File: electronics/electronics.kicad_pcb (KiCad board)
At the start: 2 copper layers, 50 parts, among them J1 USB_C_Receptacle_USB2.0_14P, J2 AMT_102, J3 SPARK_MAX, J4 BLDC_FAN_ESC, J5 Power Probes, SW1 RST, SW2 BOOT, SW3 SW_Push, SW4 SW_Push, SW5 SW_Push, SW6 SW_Push, U1 ESP32-S3-WROOM-1, U2 LSF0204, U3 NCP1117-3.3_SOT223, U4 TPS62140, U5 NCP1117-3.3_SOT223, U8 TVS1400DRV, U9 TVS1400DRV

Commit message: ready to ship out
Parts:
- added G***: LOGO, LOGO, B.Cu at (161.2, 101.2)
- added G***: LOGO, LOGO, B.Cu at (117.0, 100.9)
- added G***: LOGO, LOGO, B.Cu at (138.9, 68.7)
- added L1: 2.2uH, Inductor_SMD:L_Vishay_IHLP-1212, F.Cu at (153.8, 94.8)
- C10, C11, C4, C5, C6, C8: footprint Capacitor_SMD:C_0603_1608Metric -> Capacitor_SMD:C_0805_2012Metric
- J5: footprint Connector_PinSocket_2.54mm:PinSocket_1x06_P2.54mm_Vertical -> Connector_PinHeader_2.54mm:PinHeader_1x04_P2.54mm_Vertical
- U7: value ~ -> BMI270
- moved C5 142.2 mm to (167.8, 96.2), turned to 90 degrees
- moved R7 138.8 mm to (167.2, 70.6), turned to 90 degrees
- moved R12 135.4 mm to (173.4, 94.9), turned to 90 degrees
- moved R13 135.3 mm to (173.4, 98.1), turned to 90 degrees
- moved R5 132.4 mm to (166.4, 92.6)
- moved D3 131.7 mm to (171.7, 98.2), turned to -90 degrees
- moved D4 130.1 mm to (171.7, 94.9), turned to -90 degrees
- moved C4 129.1 mm to (155.2, 98.5), turned to -90 degrees
- moved C6 127.6 mm to (153.6, 103.3)
- moved C7 119.1 mm to (149.9, 103.1), turned to 180 degrees
- moved R9 117.7 mm to (150.6, 96.2), turned to 90 degrees
- moved R11 109.6 mm to (148.1, 99.2)
- moved R10 109.5 mm to (148.1, 97.5), turned to 180 degrees
- moved C9 105.9 mm to (136.4, 102.2), turned to -90 degrees
- moved C3 104.9 mm to (130.7, 95.7), turned to 180 degrees
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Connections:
- net Net-(L1-Pad1) renamed /POWER_INDUCTOR
- J5 pad 2: +5V -> +3V3
- J5 pad 3: +3V3 -> GND
- J5 pad 4: +3V3 -> GND
- U1 pad 15: unconnected-(U1-IO3-Pad15) -> /BTN3
- U1 pad 17: unconnected-(U1-IO9-Pad17) -> /BTN4
- U1 pad 18: unconnected-(U1-IO10-Pad18) -> /SCL
- U1 pad 19: unconnected-(U1-IO11-Pad19) -> /SDA
- U1 pad 20: unconnected-(U1-IO12-Pad20) -> /SPARK_MAX_PWM
- U1 pad 25: unconnected-(U1-IO48-Pad25) -> /BTN2
- U1 pad 26: unconnected-(U1-IO45-Pad26) -> /BTN1
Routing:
- net +3V3: track 40.4 -> 269.7 mm, vias 0 -> 6
- net +5V: track 71.7 -> 206.0 mm, vias 0 -> 7
- net /SCL: track 0.00 -> 67.0 mm, vias 0 -> 2
- net /SDA: track 0.00 -> 65.6 mm, vias 0 -> 2
- net /SPARK_MAX_PWM: track 0.00 -> 57.4 mm, vias 0 -> 2
- net /BTN2: track 0.00 -> 55.9 mm, vias 0 -> 2
- net /BTN4: track 0.00 -> 53.9 mm, vias 0 -> 2
- net Net-(U1-IO0): track 5.15 -> 46.5 mm, vias 0 -> 2
- net /BTN1: track 0.00 -> 18.2 mm
- net /BTN3: track 0.00 -> 13.7 mm
- net VBAT: track 0.00 -> 10.5 mm
- net Net-(U1-IO16): track 0.00 -> 9.59 mm
- net Net-(U1-IO46): track 0.00 -> 8.02 mm
- net GND: track 0.00 -> 5.25 mm, vias 0 -> 14
- net Net-(U1-EN): track 24.7 -> 28.9 mm
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- added copper zone on F.Cu, net +3V3
- added copper zone on F.Cu, net +5V
- added copper zone on F.Cu, net /POWER_INDUCTOR
- added copper zone on B.Cu, net GND
- added copper zone on F.Cu, net GND
- added copper zone on F.Cu, net VBAT
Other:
- board outline added: 80 x 64.8 mm
- board text added: "3V3"
- board text added: "5V"
- board text added: "GND"
- board text added: "STUYOLY TECH 2025 ELECTRIC VEHICLE MARKOVA REAWAKED KYU50"

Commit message: fix spelling
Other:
- board text added: "STUYOLY TECH 2025 ELECTRIC VEHICLE MARKOVA REAWAKENED KYU50"
- board text removed: "STUYOLY TECH 2025 ELECTRIC VEHICLE MARKOVA REAWAKED KYU50"

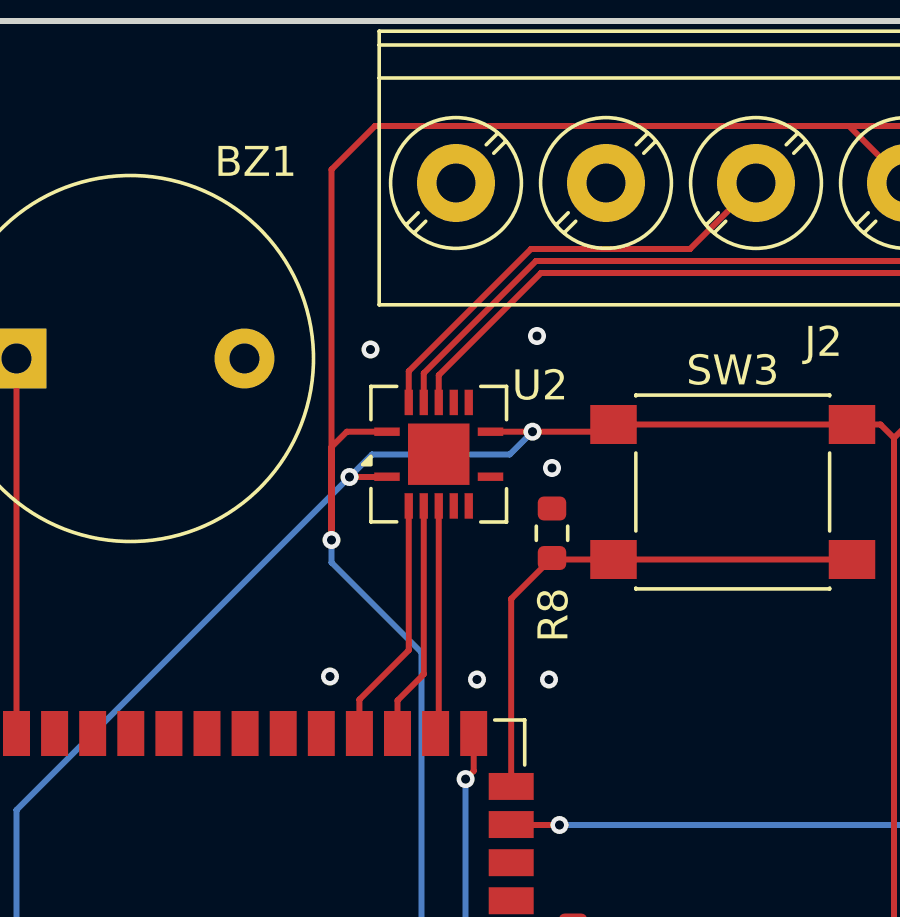
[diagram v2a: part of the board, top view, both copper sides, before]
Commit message: added laser to pcb
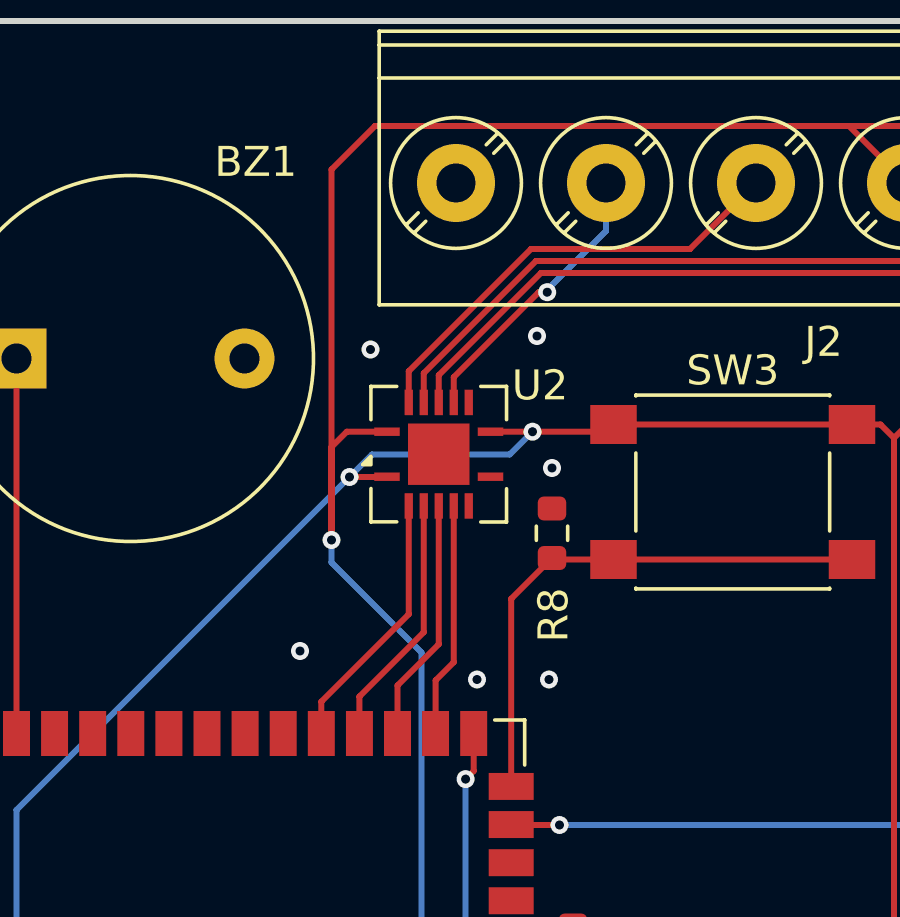
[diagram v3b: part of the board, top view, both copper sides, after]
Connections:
- J2 pad 4: /5V_ENC_INDEX -> /5V_LASER
- U1 pad 28: /3V3_FAN_PWM -> /3V3_LASER
- U1 pad 29: /3V3_ENC_B -> /3V3_FAN_PWM
- U1 pad 30: /3V3_ENC_A -> /3V3_ENC_B
- U1 pad 31: unconnected-(U1-IO38-Pad31) -> /3V3_ENC_A
- U2 pad 10: unconnected-(U2-B4-Pad10) -> /5V_LASER
- U2 pad 5: unconnected-(U2-A4-Pad5) -> /3V3_LASER
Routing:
- net /5V_LASER: track 0.00 -> 9.58 mm, vias 0 -> 1
- net /3V3_LASER: track 0.00 -> 7.98 mm
- net /3V3_ENC_A: track 8.27 -> 8.79 mm
- net /3V3_FAN_PWM: track 7.64 -> 8.16 mm
- net /3V3_ENC_B: track 7.95 -> 8.47 mm

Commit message: lgtm
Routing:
- net /5V_LASER: track 9.58 -> 10.7 mm
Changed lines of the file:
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@@
 	)
 	(segment
-		(start 126.039951 59.039951)
-		(end 125.757107 59.039951)
+		(start 125.797058 59)
+		(end 122.925 61.872058)
 		(width 0.2)
 		(layer "F.Cu")
@@
 	)
 	(segment
-		(start 125.757107 59.039951)
-		(end 122.925 61.872058)
+		(start 128 59)
+		(end 125.797058 59)
 		(width 0.2)
 		(layer "F.Cu")
@@
 	)
 	(via
-		(at 126.039951 59.039951)
+		(at 128 59)
 		(size 0.6)
 		(drill 0.3)
@@
 	)
 	(segment
-		(start 128 57)
+		(start 128 59)
 		(end 128 55.4)
 		(width 0.2)
 		(layer "B.Cu")
-		(net 17)
-	)
-	(segment
-		(start 126.039951 59.039951)
-		(end 126.039951 58.960049)
-		(width 0.2)
-		(layer "B.Cu")
-		(net 17)
-	)
-	(segment
-		(start 126.039951 58.960049)
-		(end 128 57)
-		(width 0.2)
-		(layer "B.Cu")

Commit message: transistor + ready
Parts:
- added Q1: MMBT100, Package_TO_SOT_SMD:SOT-23-3, F.Cu at (113.0, 69.2)
- added R14: 1k, Resistor_SMD:R_0603_1608Metric, F.Cu at (116.8, 68.3)
- moved BZ1 2.67 mm to (108.7, 58.6)
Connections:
- J2 pad 4: /5V_LASER -> /LASER_GND
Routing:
- net /LASER_GND: track 0.00 -> 23.0 mm, vias 0 -> 1
- net +3V3: track 269.7 -> 284.2 mm, vias 6 -> 7
- net /BUZZER: track 12.5 -> 15.3 mm
- net Net-(Q1-B): track 0.00 -> 1.80 mm
- net /5V_LASER: track 10.7 -> 12.0 mm, vias 1 -> 2
- net /5V_FAN_PWM: track 34.0 -> 34.6 mm
- net /5V_ENC_A: track 15.2 -> 15.7 mm
- net /5V_ENC_B: track 24.7 -> 25.2 mm
- net +5V: track 206.0 -> 206.1 mm, vias 7 -> 9
- net GND: vias 14 -> 13
